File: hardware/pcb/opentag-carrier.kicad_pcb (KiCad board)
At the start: 2 copper layers, 10 parts

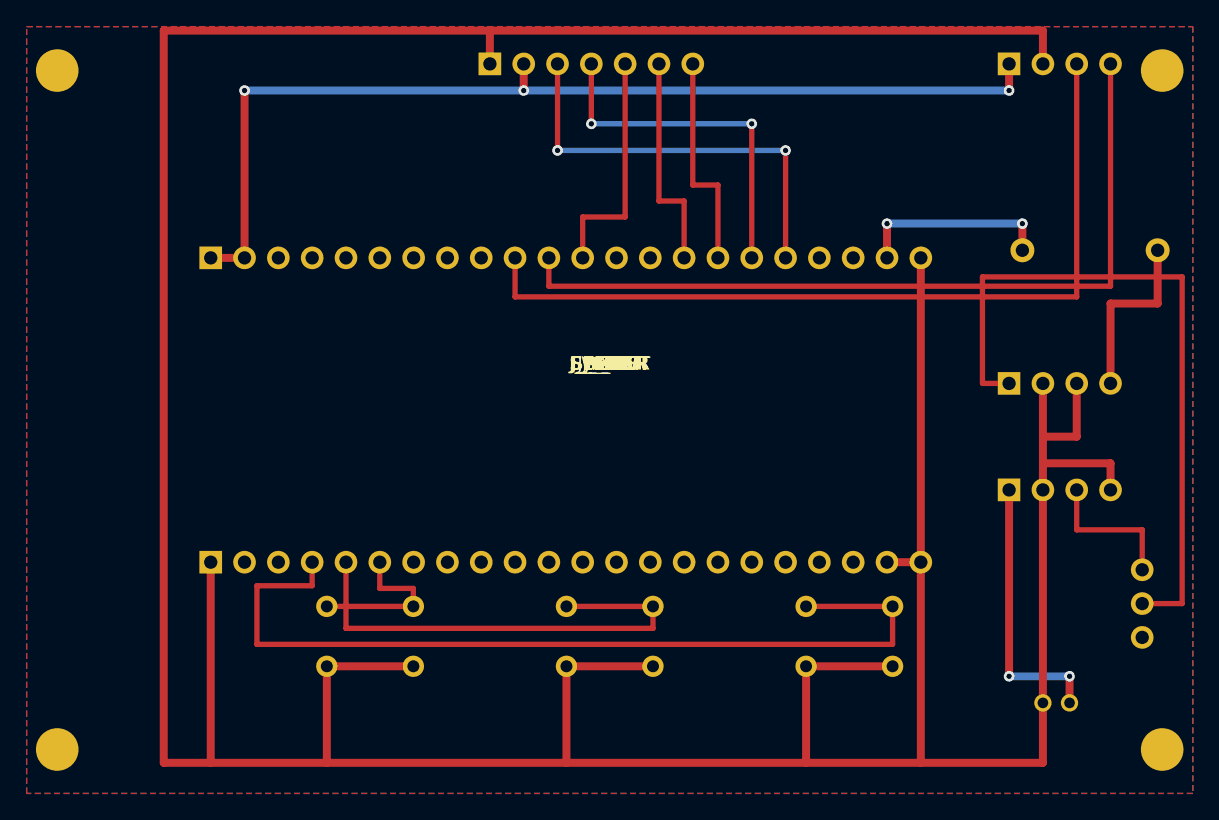
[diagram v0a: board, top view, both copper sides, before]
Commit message: Add BACK button (GPIO13) end-to-end; fix preview hover bug; self-explanatory UIs
Hardware: 4th tactile (BACK) on J1-19/GPIO13 — the repurposed SPI MISO pin,
since the OLED bus is write-only. Carrier PCB regenerates with a centred
4-button row (16.5 mm pitch): UP stays on F.Cu, DOWN/OK hop to B.Cu on
stacked lanes, BACK crosses the socket's east end on B.Cu; self-checks pass
(90 pads, 89 tracks, 18 vias). Shell CAD + STLs: four button holes, cap
print count 4. Docs updated (WIRING, BOM, HARDWARE, README).

Firmware: btnBack handled in every UI state — cancels tag-scan/write, stops
emulation, skips lock confirm, and gives the populated amiibo library its
first exit path back to the menu. SPI.begin no longer claims GPIO13. New
NOTE:CLEAR BLE command so the web page's clear button actually clears.
Screen hints rewritten around BACK; 'Clear note' renamed 'Clear NDEF note'.

Web preview: hover-across-a-button no longer presses it (mouseleave only
cancels the pending press; a press fires on real mouseup/touchend only).
BACK button + Backspace/Left-arrow keys, all screens re-ported 1:1 from
drawScreen() (pixel-verified: pvtest2 23/23, behaviour harness 41/41).

Web sync: 'Clear device note' now sends NOTE:CLEAR; new 'Amiibo database'
browser (search + lazy box art + series/type/year, no connection needed);
NDEF note card explains the whole note flow step by step.

Co-authored-by: arena-agent <297053741+arena-agent@users.noreply.github.com>
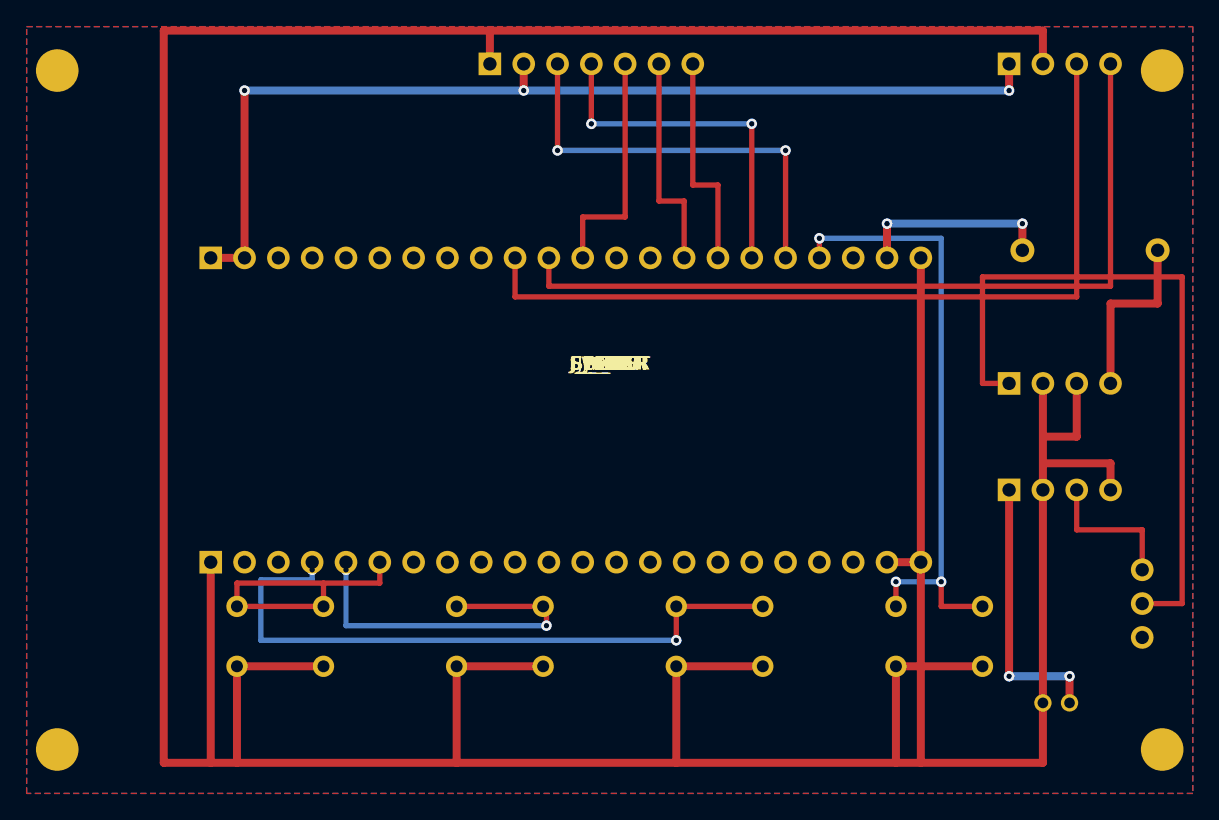
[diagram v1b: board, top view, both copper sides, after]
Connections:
- J_DEVKIT pad J1-19: (no net) -> BTN_BACK
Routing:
- net BTN_BACK: track 0.00 -> 46.6 mm, vias 0 -> 3
- net BTN_OK: track 67.4 -> 50.0 mm, vias 0 -> 2
- net GND: track 331.0 -> 344.7 mm
- net BTN_UP: track 12.3 -> 22.3 mm
- net BTN_DOWN: track 36.2 -> 28.0 mm, vias 0 -> 2
